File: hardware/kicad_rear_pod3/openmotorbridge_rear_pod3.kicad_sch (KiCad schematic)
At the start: 0 parts

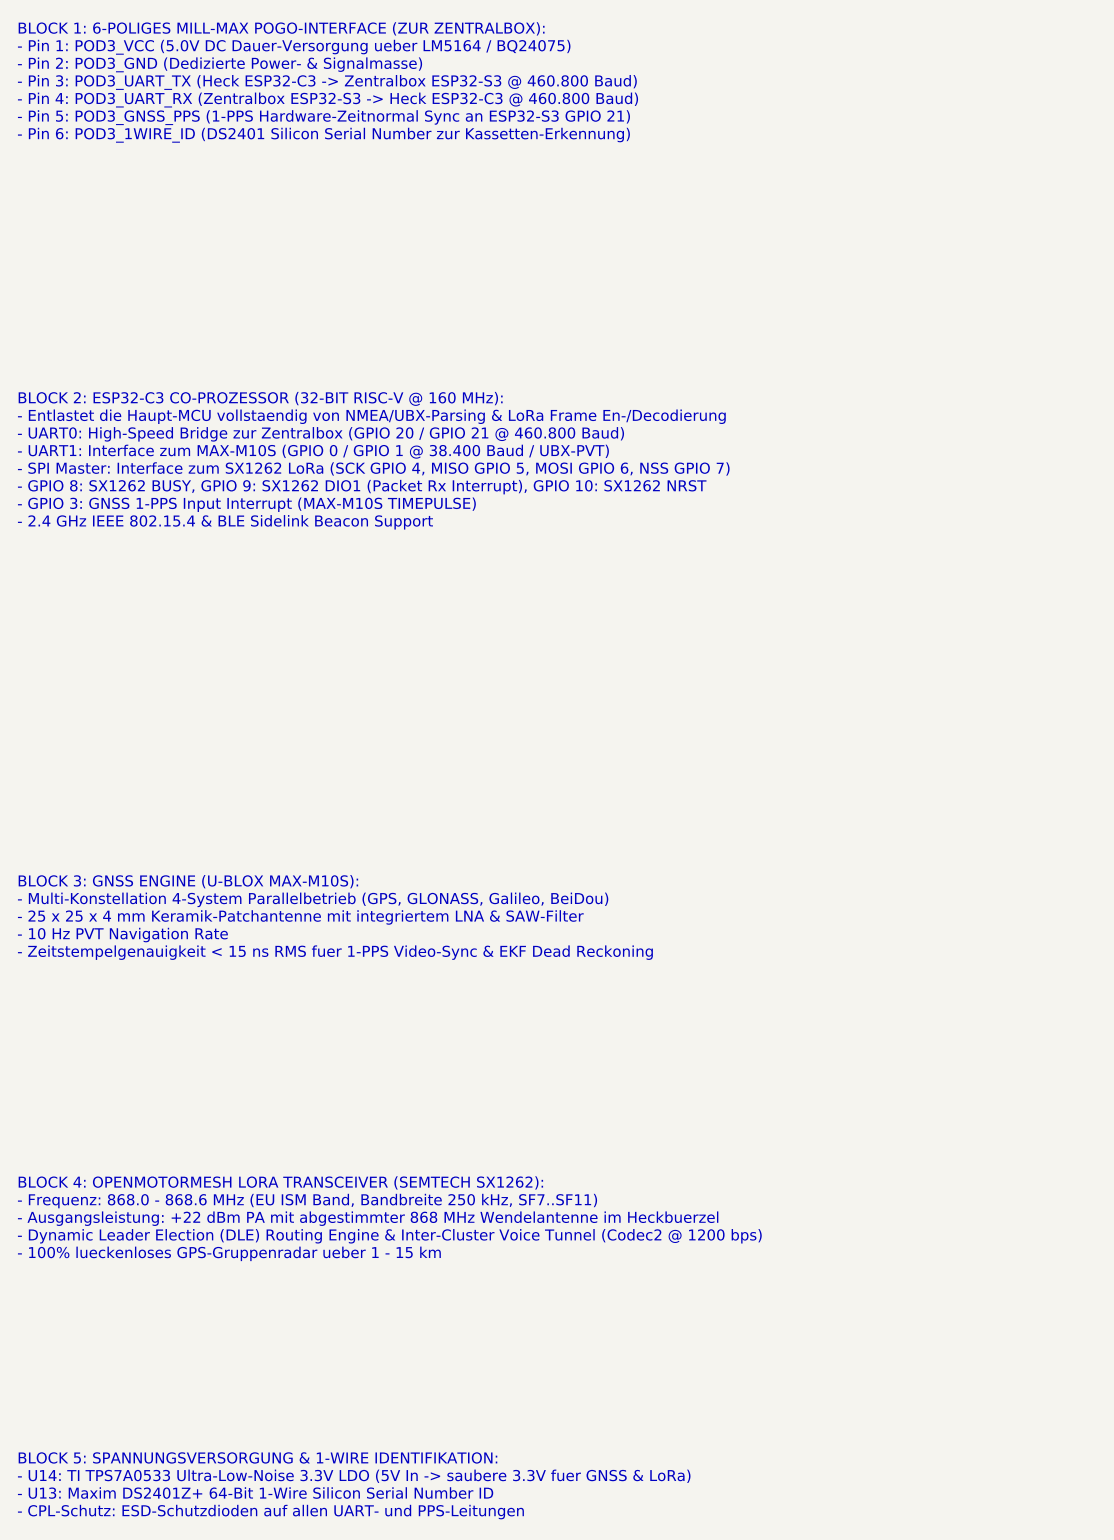
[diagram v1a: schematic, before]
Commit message: fix(dual-phy): Explicitly document and initialize both 2.4 GHz Primary Mesh and 868 MHz LoRa Fallback in Rear Pod 3
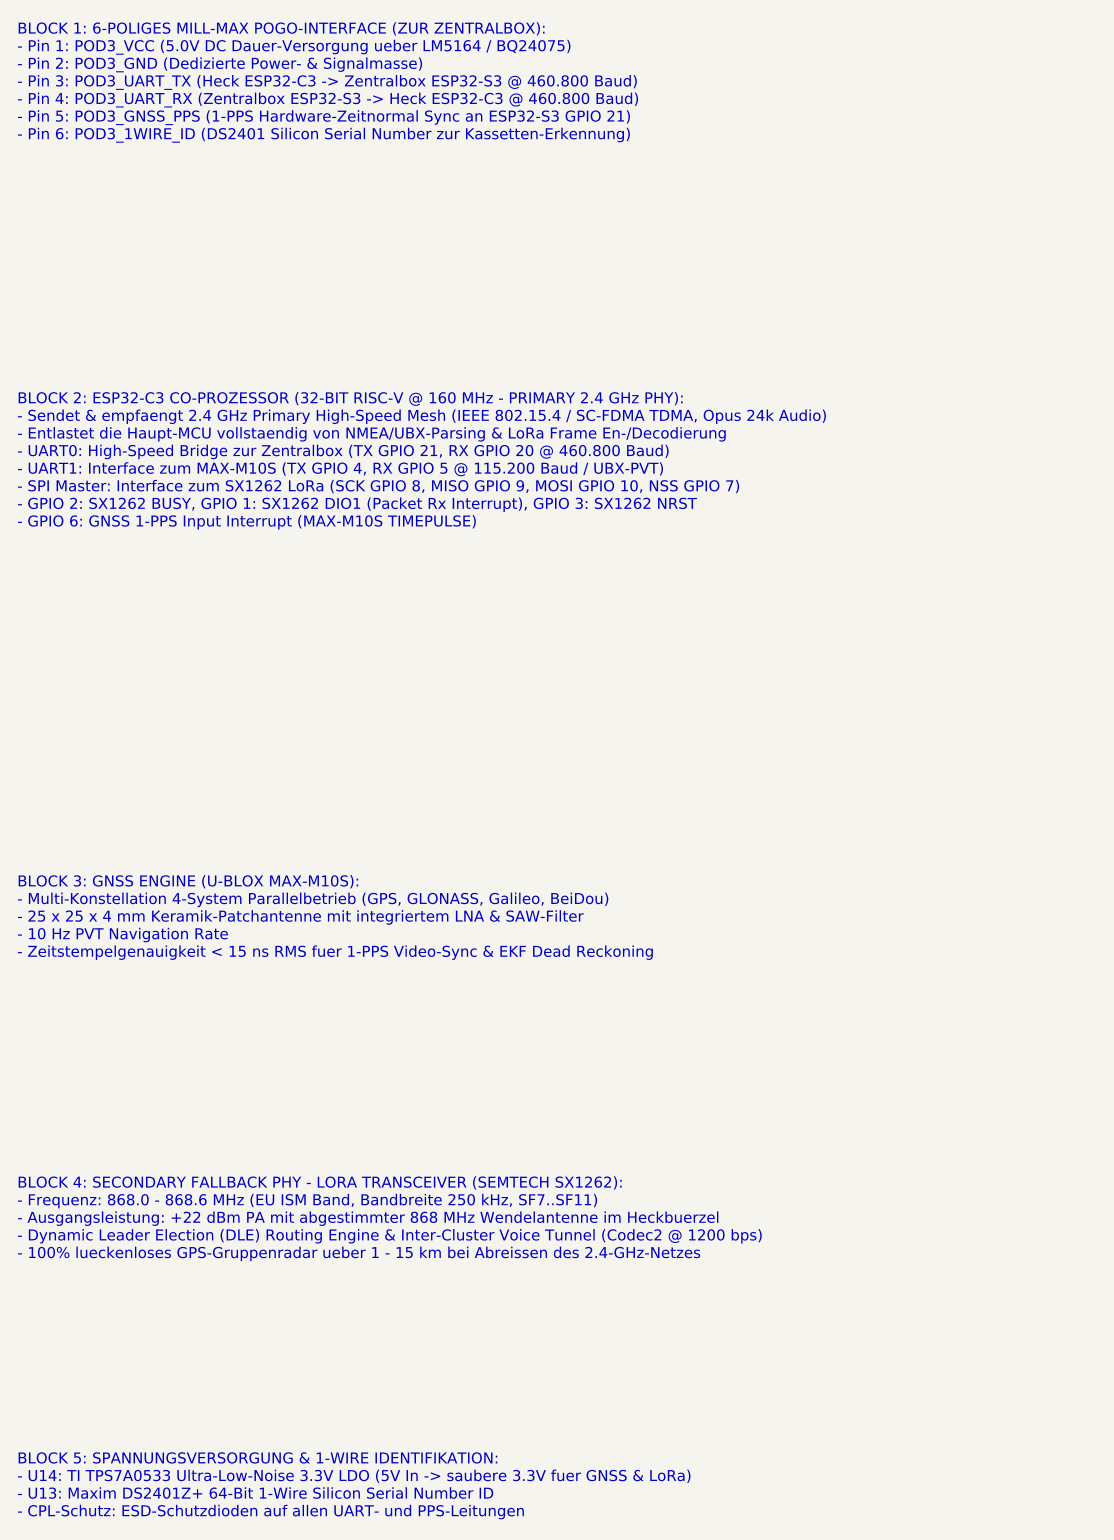
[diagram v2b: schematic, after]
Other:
- note added: "BLOCK 2: ESP32-C3 CO-PROZESSOR (32-BIT RISC-V @ 160 MHz - PRIMARY 2.4 GHz PHY): - Sendet & empfaengt 2.4 GHz Primary High-Speed Mesh (IEEE 802.15.4 / SC-FDMA TDMA, Opus 24k Audio) - Entlastet die Haupt-MCU vollstaendig von NMEA/UBX-Parsing & LoRa Frame En-/Decodierung - UART0: High-Speed Bridge zur Zentralbox (TX GPIO 21, RX GPIO 20 @ 460.800 Baud) - UART1: Interface zum MAX-M10S (TX GPIO 4, RX G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"
- note added: "BLOCK 4: SECONDARY FALLBACK PHY - LORA TRANSCEIVER (SEMTECH SX1262): - Frequenz: 868.0 - 868.6 MHz (EU ISM Band, Bandbreite 250 kHz, SF7..SF11) - Ausgangsleistung: +22 dBm PA mit abgestimmter 868 MHz Wendelantenne im Heckbuerzel - Dynamic Leader Election (DLE) Routing Engine & Inter-Cluster Voice Tunnel (Codec2 @ 1200 bps) - 100% lueckenloses GPS-Gruppenradar ueber 1 - 15 km bei Abreissen des 2.4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"
- note removed: "BLOCK 2: ESP32-C3 CO-PROZESSOR (32-BIT RISC-V @ 160 MHz): - Entlastet die Haupt-MCU vollstaendig von NMEA/UBX-Parsing & LoRa Frame En-/Decodierung - UART0: High-Speed Bridge zur Zentralbox (GPIO 20 / GPIO 21 @ 460.800 Baud) - UART1: Interface zum MAX-M10S (GPIO 0 / GPIO 1 @ 38.400 Baud / UBX-PVT) - SPI Master: Interface zum SX1262 LoRa (SCK GPIO 4, MISO GPIO 5, MOSI GPIO 6, NSS GPIO 7) - GPIO 8: 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"
- note removed: "BLOCK 4: OPENMOTORMESH LORA TRANSCEIVER (SEMTECH SX1262): - Frequenz: 868.0 - 868.6 MHz (EU ISM Band, Bandbreite 250 kHz, SF7..SF11) - Ausgangsleistung: +22 dBm PA mit abgestimmter 868 MHz Wendelantenne im Heckbuerzel - Dynamic Leader Election (DLE) Routing Engine & Inter-Cluster Voice Tunnel (Codec2 @ 1200 bps) - 100% lueckenloses GPS-Gruppenradar ueber 1 - 15 km"
- title: OpenMotorBridge v8.0 - Heck-Pod 3 (GNSS & OpenMotorMesh LoRa) -> OpenMotorBridge v8.0 - Heck-Pod 3 (GNSS & Dual-PHY OpenMotorMesh)
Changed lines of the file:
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@@
   (paper "A3")
   (title_block
-    (title "OpenMotorBridge v8.0 - Heck-Pod 3 (GNSS & OpenMotorMesh LoRa)")
+    (title "OpenMotorBridge v8.0 - Heck-Pod 3 (GNSS & Dual-PHY OpenMotorMesh)")
     (date "2026-08-23")
     (rev "v8.0")
     (company "OpenMotorBridge Open Source Hardware")
-    (comment 1 "u-blox MAX-M10S 10Hz GNSS + Semtech SX1262 LoRa (+22 dBm @ 868 MHz)")
-    (comment 2 "ESP32-C3 RISC-V Co-Prozessor + DS2401 1-Wire ID + 6-Pin Pogo Interface")
+    (comment 1 "u-blox MAX-M10S 10Hz GNSS + ESP32-C3 2.4GHz Mesh + Semtech SX1262 LoRa (+22 dBm @ 868 MHz)")
+    (comment 2 "Dual-PHY OMM Transceiver: 2.4 GHz HiFi Primary + 868 MHz Long-Range Fallback")
   )
   (text "BLOCK 1: 6-POLIGES MILL-MAX POGO-INTERFACE (ZUR ZENTRALBOX):\n- Pin 1: POD3_VCC (5.0V DC Dauer-Versorgung ueber LM5164 / BQ24075)\n- Pin 2: POD3_GND (Dedizierte Power- & Signalmasse)\n- Pin 3: POD3_UART_TX (Heck ESP32-C3 -> Zentralbox ESP32-S3 @ 460.800 Baud)\n- Pin 4: POD3_UART_RX (Zentralbox ESP32-S3 -> Heck ESP32-C3 @ 460.800 Baud)\n- Pin 5: POD3_GNSS_PPS (1-PPS Hardware-Zeitnormal Sync an ESP32-S3 GPIO 21)\n- Pin 6: POD3_1WIRE_ID (DS2401 Silicon Serial Number zur Kassetten-Erkennung)" (at 25.4 45.0 0)
     (effects (font (size 1.27 1.27)) (justify left bottom))
   )
-  (text "BLOCK 2: ESP32-C3 CO-PROZESSOR (32-BIT RISC-V @ 160 MHz):\n- Entlastet die Haupt-MCU vollstaendig von NMEA/UBX-Parsing & LoRa Frame En-/Decodierung\n- UART0: High-Speed Bridge zur Zentralbox (GPIO 20 / GPIO 21 @ 460.800 Baud)\n- UART1: Interface zum MAX-M10S (GPIO 0 / GPIO 1 @ 38.400 Baud / UBX-PVT)\n- SPI Master: Interface zum SX1262 LoRa (SCK GPIO 4, MISO GPIO 5, MOSI GPIO 6, NSS GPIO 7)\n- GPIO 8: SX1262 BUSY, GPIO 9: SX1262 DIO1 (Packet Rx Interrupt), GPIO 10: SX1262 NRST\n- GPIO 3: GNSS 1-PPS Input Interrupt (MAX-M10S TIMEPULSE)\n- 2.4 GHz IEEE 802.15.4 & BLE Sidelink Beacon Support" (at 25.4 90.0 0)
+  (text "BLOCK 2: ESP32-C3 CO-PROZESSOR (32-BIT RISC-V @ 160 MHz - PRIMARY 2.4 GHz PHY):\n- Sendet & empfaengt 2.4 GHz Primary High-Speed Mesh (IEEE 802.15.4 / SC-FDMA TDMA, Opus 24k Audio)\n- Entlastet die Haupt-MCU vollstaendig von NMEA/UBX-Parsing & LoRa Frame En-/Decodierung\n- UART0: High-Speed Bridge zur Zentralbox (TX GPIO 21, RX GPIO 20 @ 460.800 Baud)\n- UART1: Interface zum MAX-M10S (TX GPIO 4, RX GPIO 5 @ 115.200 Baud / UBX-PVT)\n- SPI Master: Interface zum SX1262 LoRa (SCK GPIO 8, MISO GPIO 9, MOSI GPIO 10, NSS GPIO 7)\n- GPIO 2: SX1262 BUSY, GPIO 1: SX1262 DIO1 (Packet Rx Interrupt), GPIO 3: SX1262 NRST\n- GPIO 6: GNSS 1-PPS Input Interrupt (MAX-M10S TIMEPULSE)" (at 25.4 90.0 0)
     (effects (font (size 1.27 1.27)) (justify left bottom))
   )
@@
     (effects (font (size 1.27 1.27)) (justify left bottom))
   )
-  (text "BLOCK 4: OPENMOTORMESH LORA TRANSCEIVER (SEMTECH SX1262):\n- Frequenz: 868.0 - 868.6 MHz (EU ISM Band, Bandbreite 250 kHz, SF7..SF11)\n- Ausgangsleistung: +22 dBm PA mit abgestimmter 868 MHz Wendelantenne im Heckbuerzel\n- Dynamic Leader Election (DLE) Routing Engine & Inter-Cluster Voice Tunnel (Codec2 @ 1200 bps)\n- 100% lueckenloses GPS-Gruppenradar ueber 1 - 15 km" (at 25.4 175.0 0)
+  (text "BLOCK 4: SECONDARY FALLBACK PHY - LORA TRANSCEIVER (SEMTECH SX1262):\n- Frequenz: 868.0 - 868.6 MHz (EU ISM Band, Bandbreite 250 kHz, SF7..SF11)\n- Ausgangsleistung: +22 dBm PA mit abgestimmter 868 MHz Wendelantenne im Heckbuerzel\n- Dynamic Leader Election (DLE) Routing Engine & Inter-Cluster Voice Tunnel (Codec2 @ 1200 bps)\n- 100% lueckenloses GPS-Gruppenradar ueber 1 - 15 km bei Abreissen des 2.4-GHz-Netzes" (at 25.4 175.0 0)
     (effects (font (size 1.27 1.27)) (justify left bottom))
   )
